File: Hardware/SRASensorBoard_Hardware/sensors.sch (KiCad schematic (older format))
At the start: 53 parts, among them J1 USB_A, Q1 BSS138, Q2 BSS138, Q3 BSS138, Q4 BSS138, Q5 BSS138, Q6 BSS138, U4 FT230XS

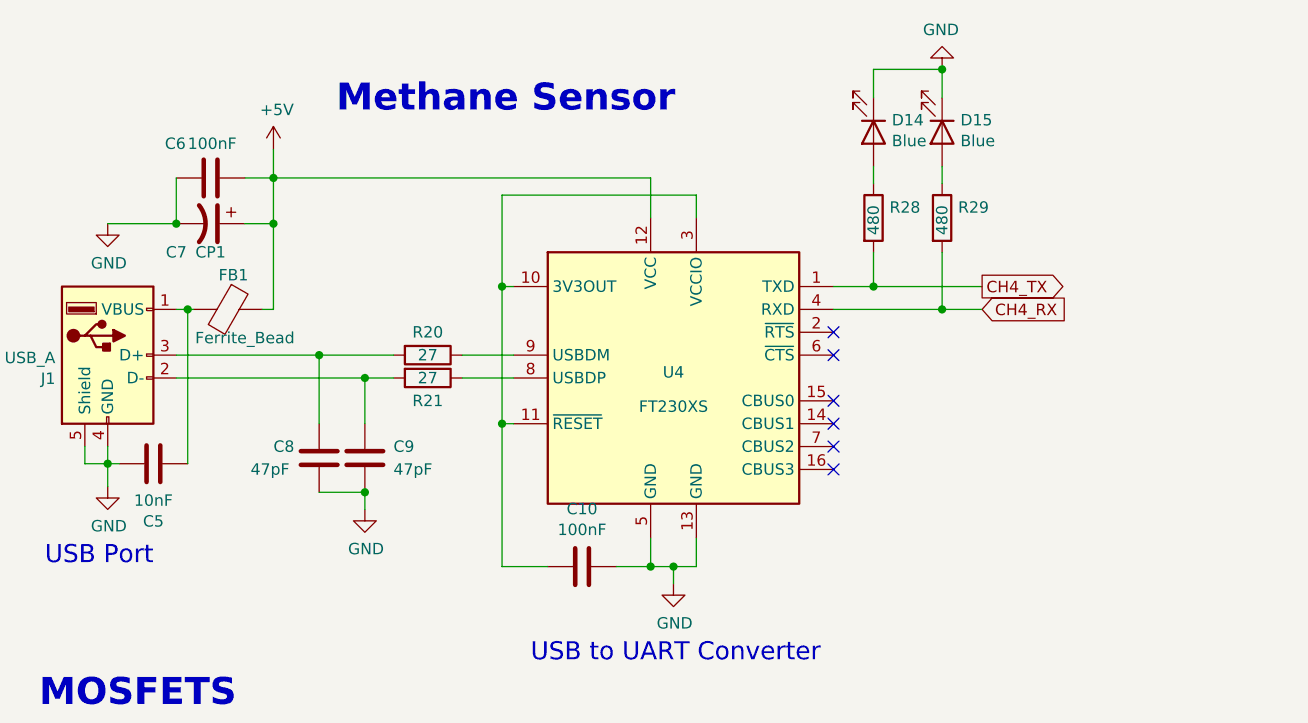
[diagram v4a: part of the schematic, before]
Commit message: Flipped ground symbol
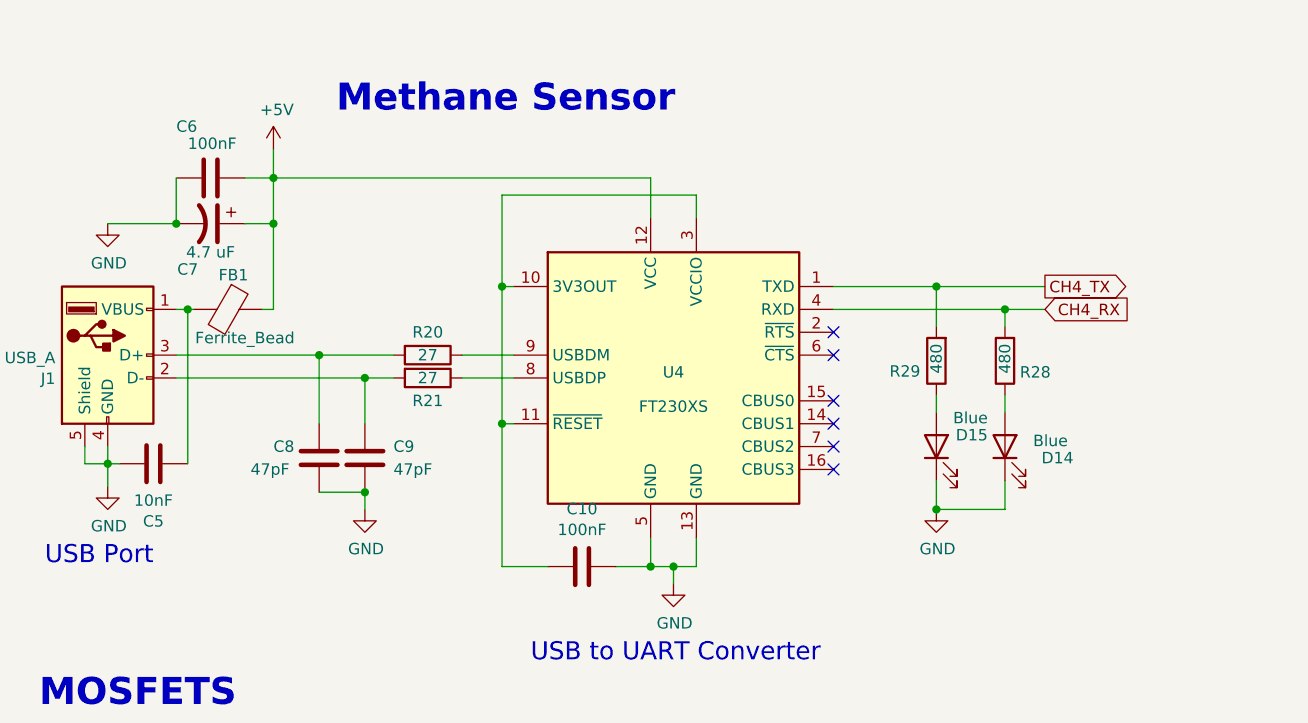
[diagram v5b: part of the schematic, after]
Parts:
- C7: value CP1 -> 4.7 uF
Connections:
- net CH4_RX: now also R28.2; no longer R29.2
- net CH4_TX: now also R29.2; no longer R28.2
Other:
- moved on the sheet: D14, D15, R28, R29
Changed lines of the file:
@@
 	4325 2125 5150 2125
-Wire Wire Line
-	6400 1425 6400 1250
 Wire Wire Line
 	6400 1250 4750 1250
@@
 $EndComp
 Wire Wire Line
-	6600 1425 6600 1325
-Wire Wire Line
 	5800 1725 5750 1725
 Wire Wire Line
@@
 U 1 1 6167C537
 P 4475 1250
-F 0 "C6" V 4325 1050 50  0000 L CNN
+F 0 "C6" V 4250 1100 50  0000 L CNN
 F 1 "100nF" V 4325 1150 50  0000 L CNN
 F 2 "" H 4513 1100 50  0001 C CNN
@@
 U 1 1 61685AB6
 P 4475 1450
-F 0 "C7" V 4600 1300 50  0000 C CNN
-F 1 "CP1" V 4600 1450 50  0000 C CNN
+F 0 "C7" V 4675 1350 50  0000 C CNN
+F 1 "4.7 uF" V 4600 1450 50  0000 C CNN
 F 2 "" H 4475 1450 50  0001 C CNN
 F 3 "~" H 4475 1450 50  0001 C CNN
@@
 $EndComp
 Connection ~ 4325 1450
-Wire Wire Line
-	7200 1725 7375 1725
-Wire Wire Line
-	7200 1825 7675 1825
-$Comp
-L Device:R R28
-U 1 1 6168B9AC
-P 7375 1425
-F 0 "R28" H 7445 1471 50  0000 L CNN
-F 1 "480" V 7375 1350 50  0000 L CNN
-F 2 "" V 7305 1425 50  0001 C CNN
-F 3 "~" H 7375 1425 50  0001 C CNN
-	1    7375 1425
-	1    0    0    -1
-$EndComp
-$Comp
-L Device:R R29
-U 1 1 6168BDE5
-P 7675 1425
-F 0 "R29" H 7745 1471 50  0000 L CNN
-F 1 "480" V 7675 1350 50  0000 L CNN
-F 2 "" V 7605 1425 50  0001 C CNN
-F 3 "~" H 7675 1425 50  0001 C CNN
-	1    7675 1425
-	1    0    0    -1
-$EndComp
-$Comp
-L Device:LED D14
-U 1 1 6168C4BA
-P 7375 1050
-F 0 "D14" V 7322 1130 50  0000 L CNN
-F 1 "Blue" V 7413 1130 50  0000 L CNN
-F 2 "" H 7375 1050 50  0001 C CNN
-F 3 "~" H 7375 1050 50  0001 C CNN
-	1    7375 1050
-	0    1    1    0
-$EndComp
-$Comp
-L Device:LED D15
-U 1 1 6168D01D
-P 7675 1050
-F 0 "D15" V 7622 1130 50  0000 L CNN
-F 1 "Blue" V 7713 1130 50  0000 L CNN
-F 2 "" H 7675 1050 50  0001 C CNN
-F 3 "~" H 7675 1050 50  0001 C CNN
-	1    7675 1050
-	0    1    1    0
-$EndComp
-$Comp
-L power:GND #PWR0134
-U 1 1 61690493
-P 7675 775
-F 0 "#PWR0134" H 7675 525 50  0001 C CNN
-F 1 "GND" H 7680 602 50  0000 C CNN
-F 2 "" H 7675 775 50  0001 C CNN
-F 3 "" H 7675 775 50  0001 C CNN
-	1    7675 775
-	-1   0    0    1
-$EndComp
-Wire Wire Line
-	7375 1725 7375 1575
-Connection ~ 7375 1725
-Wire Wire Line
-	7375 1725 7850 1725
-Wire Wire Line
-	7375 1275 7375 1200
-Wire Wire Line
-	7375 900  7375 775
-Wire Wire Line
-	7375 775  7675 775
-Wire Wire Line
-	7675 900  7675 775
-Connection ~ 7675 775
-Wire Wire Line
-	7675 1200 7675 1275
-Wire Wire Line
-	7675 1575 7675 1825
-Connection ~ 7675 1825
-Wire Wire Line
-	7675 1825 7850 1825
 Connection ~ 5150 2625
 Wire Wire Line
@@
 Text GLabel 7225 4475 0    50   Input ~ 0
 CH4_TX
-Text GLabel 7850 1725 2    50   Output ~ 0
-CH4_TX
-Text GLabel 7850 1825 2    50   Input ~ 0
-CH4_RX
 Text GLabel 7550 4475 2    50   Output ~ 0
 TIVA_CH4_RX
@@
 Wire Wire Line
 	5575 2025 5800 2025
+NoConn ~ 7200 2225
+NoConn ~ 7200 2325
+NoConn ~ 7200 2425
+NoConn ~ 7200 2525
+NoConn ~ 7200 2025
+NoConn ~ 7200 1925
+Wire Wire Line
+	6600 1425 6600 1325
+Wire Wire Line
+	6400 1425 6400 1250
 $Comp
 L Interface_USB:FT230XS U4
@@
 	1    0    0    -1
 $EndComp
-NoConn ~ 7200 2225
-NoConn ~ 7200 2325
-NoConn ~ 7200 2425
-NoConn ~ 7200 2525
-NoConn ~ 7200 2025
-NoConn ~ 7200 1925
+Wire Wire Line
+	7950 1825 8125 1825
+Connection ~ 7950 1825
+Wire Wire Line
+	7950 1825 7950 1900
+Wire Wire Line
+	7650 1725 8125 1725
+Connection ~ 7650 1725
+Wire Wire Line
+	7650 1725 7650 1900
+Wire Wire Line
+	7200 1725 7650 1725
+Wire Wire Line
+	7200 1825 7950 1825
+$Comp
+L Device:R R28
+U 1 1 6168B9AC
+P 7950 2050
+F 0 "R28" H 7750 2100 50  0000 L CNN
+F 1 "480" V 7950 1975 50  0000 L CNN
+F 2 "" V 7880 2050 50  0001 C CNN
+F 3 "~" H 7950 2050 50  0001 C CNN
+	1    7950 2050
+	-1   0    0    1
+$EndComp
+$Comp
+L Device:R R29
+U 1 1 6168BDE5
+P 7650 2050
+F 0 "R29" H 7720 2096 50  0000 L CNN
+F 1 "480" V 7650 1975 50  0000 L CNN
+F 2 "" V 7580 2050 50  0001 C CNN
+F 3 "~" H 7650 2050 50  0001 C CNN
+	1    7650 2050
+	-1   0    0    1
+$EndComp
+$Comp
+L Device:LED D14
+U 1 1 6168C4BA
+P 7950 2425
+F 0 "D14" V 7900 2125 50  0000 L CNN
+F 1 "Blue" V 7975 2150 50  0000 L CNN
+F 2 "" H 7950 2425 50  0001 C CNN
+F 3 "~" H 7950 2425 50  0001 C CNN
+	1    7950 2425
+	0    -1   -1   0
+$EndComp
+$Comp
+L Device:LED D15
+U 1 1 6168D01D
+P 7650 2425
+F 0 "D15" V 7700 2200 50  0000 L CNN
+F 1 "Blue" V 7775 2200 50  0000 L CNN
+F 2 "" H 7650 2425 50  0001 C CNN
+F 3 "~" H 7650 2425 50  0001 C CNN
+	1    7650 2425
+	0    -1   -1   0
+$EndComp
+$Comp
+L power:GND #PWR0134
+U 1 1 61690493
+P 7650 2700
+F 0 "#PWR0134" H 7650 2450 50  0001 C CNN
+F 1 "GND" H 7655 2527 50  0000 C CNN
+F 2 "" H 7650 2700 50  0001 C CNN
+F 3 "" H 7650 2700 50  0001 C CNN
+	1    7650 2700
+	1    0    0    -1
+$EndComp
+Wire Wire Line
+	7950 2200 7950 2275
+Wire Wire Line
+	7950 2575 7950 2700
+Wire Wire Line
+	7950 2700 7650 2700
+Wire Wire Line
+	7650 2575 7650 2700
+Connection ~ 7650 2700
+Wire Wire Line
+	7650 2275 7650 2200
+Text GLabel 8125 1825 2    50   Input ~ 0
+CH4_RX
+Text GLabel 8125 1725 2    50   Output ~ 0
+CH4_TX
 $EndSCHEMATC

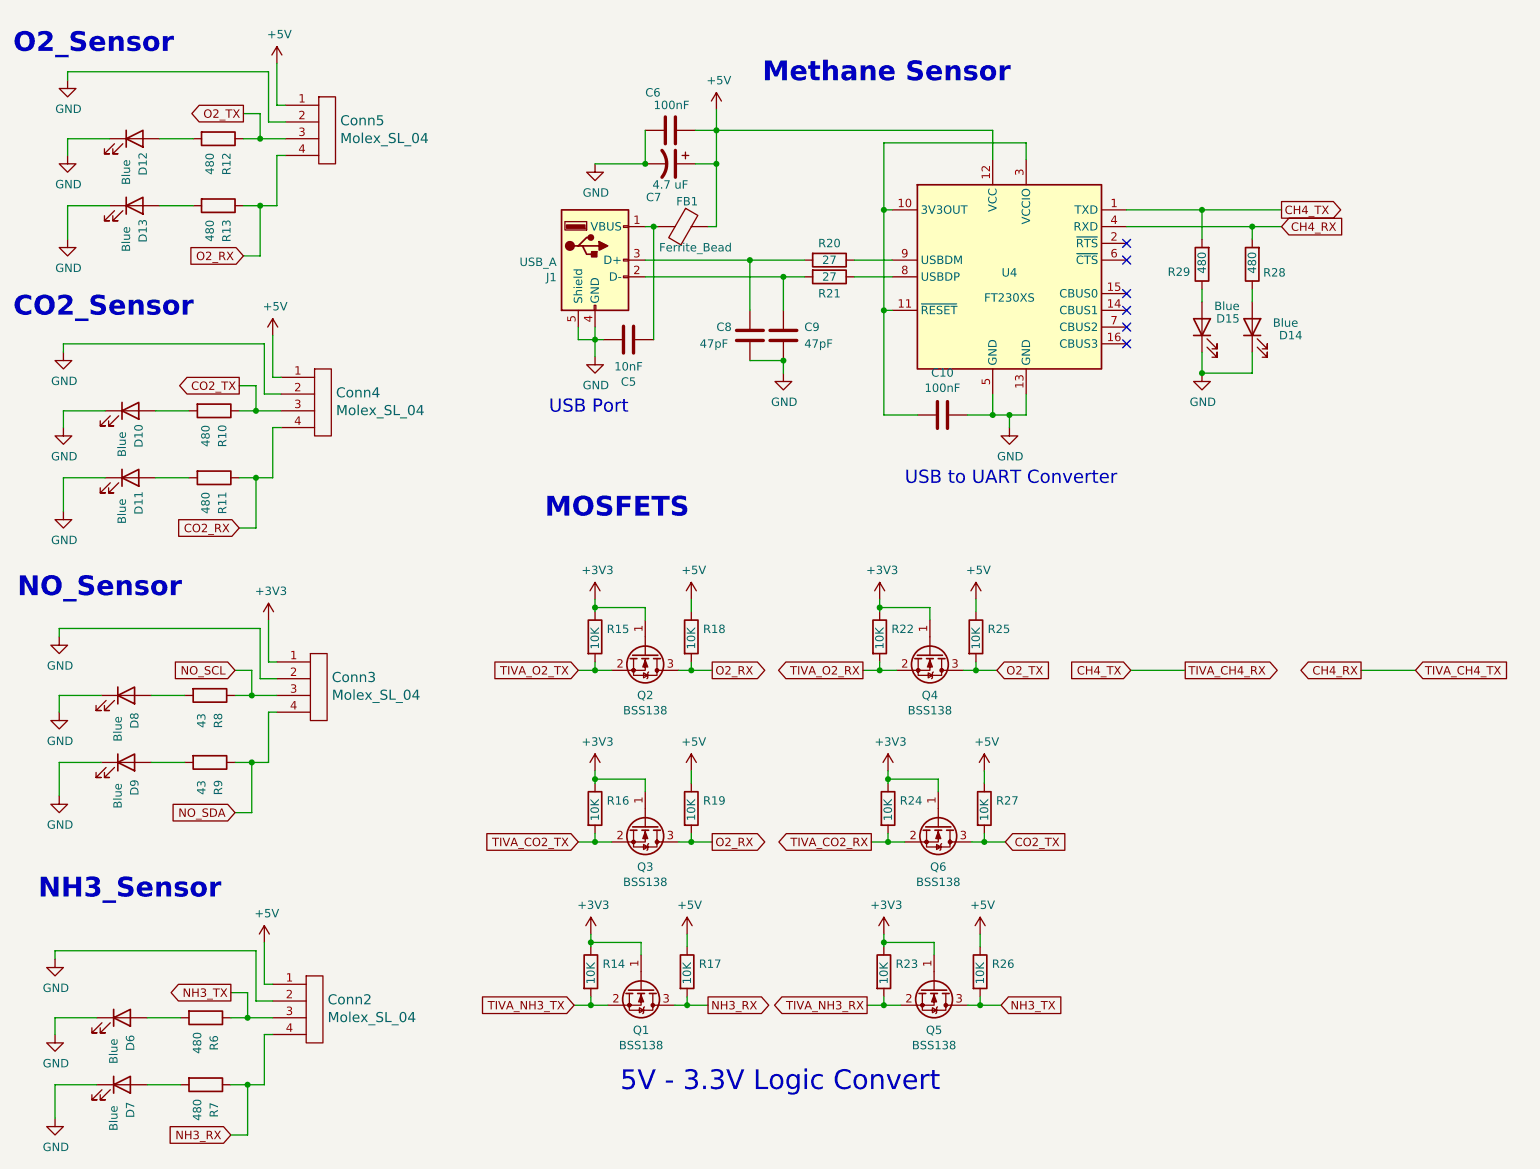
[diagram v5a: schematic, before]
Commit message: Footprint, Layout started
Replaced each 480 ohm resistor with 2 240 ohm resistors b/c we could not find 480 in stock. Footprints for board filled out. Organized components that need to be connected near each other, board placement and wires still need to be done. Board outline created.
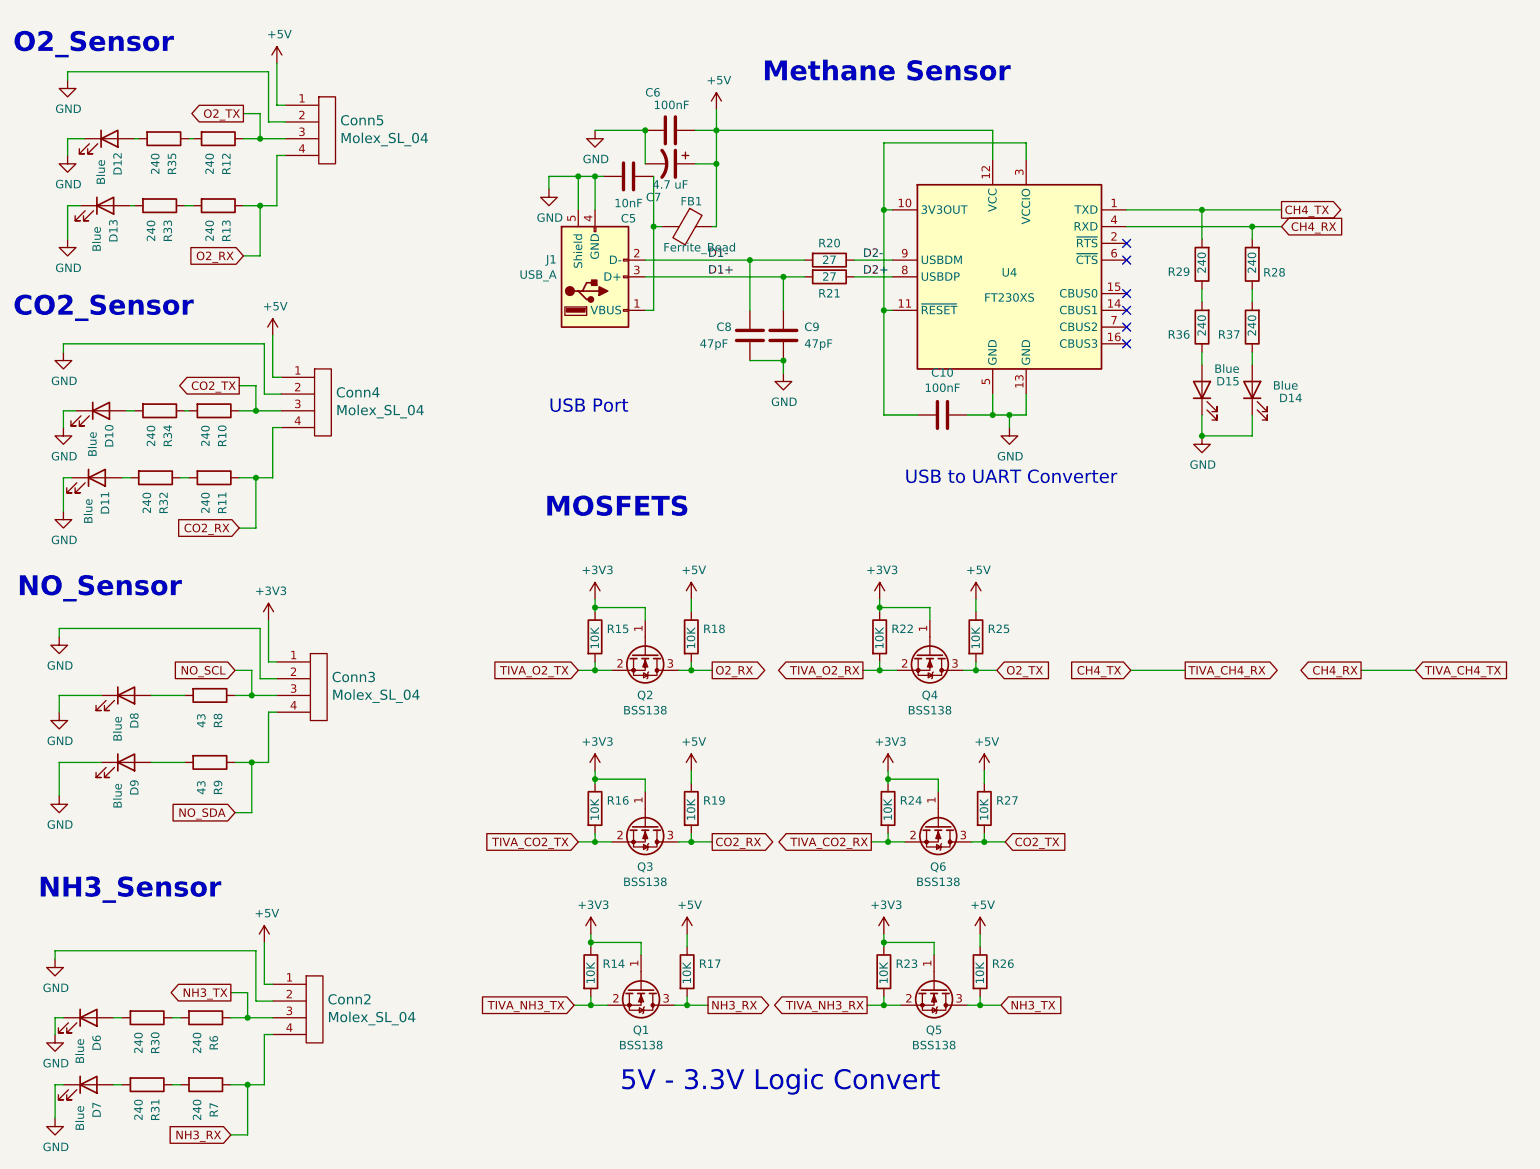
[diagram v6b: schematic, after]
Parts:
- added R30, R31, R32, R33, R34, R35, R36, R37: 240, Resistor_SMD:R_0603_1608Metric_Pad1.05x0.95mm_HandSolder, symbol Device:R
- C10, C5, C6, C7: footprint (none) -> Capacitor_SMD:C_0603_1608Metric_Pad1.05x0.95mm_HandSolder
- C8, C9: footprint (none) -> Capacitor_SMD:C_01005_0402Metric
- Conn2, Conn3, Conn4, Conn5: footprint (none) -> MRDT_Connectors:MOLEX_SL_04_Horizontal
- D10, D11, D12, D13, D14, D15, D6, D7, D8, D9: footprint (none) -> LED_SMD:LED_0603_1608Metric_Pad1.05x0.95mm_HandSolder
- FB1: footprint (none) -> Resistor_SMD:R_0805_2012Metric_Pad1.15x1.40mm_HandSolder
- J1: footprint (none) -> Connector_USB:USB_A_Stewart_SS-52100-001_Horizontal
- R10, R11, R12, R13, R28, R29, R6, R7: value 480 -> 240; footprint (none) -> Resistor_SMD:R_0603_1608Metric_Pad1.05x0.95mm_HandSolder
- R14, R15, R16, R17, R18, R19, R20, R21, R22, R23, R24, R25, R26, R27, R8, R9: footprint (none) -> Resistor_SMD:R_0603_1608Metric_Pad1.05x0.95mm_HandSolder
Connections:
- net CO2_RX: now also Q3.3 (D), R19.2
- net O2_RX: no longer Q3.3 (D), R19.2
- net D2+: now reaches R21.1, U4.8 (USBDP)
- net D2-: now reaches R20.1, U4.9 (USBDM)
- net at R12.2: now also R35.1; no longer D12.2 (A)
- net at R13.2: now also R33.1; no longer D13.2 (A)
- net at R10.2: now also R34.1; no longer D10.2 (A)
- net at R11.2: now also R32.1; no longer D11.2 (A)
- net D1+: now reaches C9.1, R21.2
- net D1+: now also J1.3 (D+); no longer J1.2 (D-)
- net D1-: now reaches C8.1, R20.2
- net D1-: now also J1.2 (D-); no longer J1.3 (D+)
- net at R28.1: now also R37.2; no longer D14.2 (A)
- net at R29.1: now also R36.2; no longer D15.2 (A)
- net at R6.2: now also R30.1; no longer D6.2 (A)
- net at R7.2: now also R31.1; no longer D7.2 (A)
- new net: D12.2 (A), R35.2
- new net: D13.2 (A), R33.2
- new net: D10.2 (A), R34.2
- new net: D11.2 (A), R32.2
- new net: D14.2 (A), R37.1
- new net: D15.2 (A), R36.1
- new net: D6.2 (A), R30.2
- new net: D7.2 (A), R31.2
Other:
- moved on the sheet: C5, D10, D11, D12, D13, D14, D15, D6, D7, FB1
